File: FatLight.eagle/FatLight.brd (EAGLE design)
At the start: 75 x 100 mm, 27 parts, among them J1 12V, Q1 IRF540, Q2 IRF540, Q3 IRF540, Q4 16MHz, U1 ATMEGA328P-PU

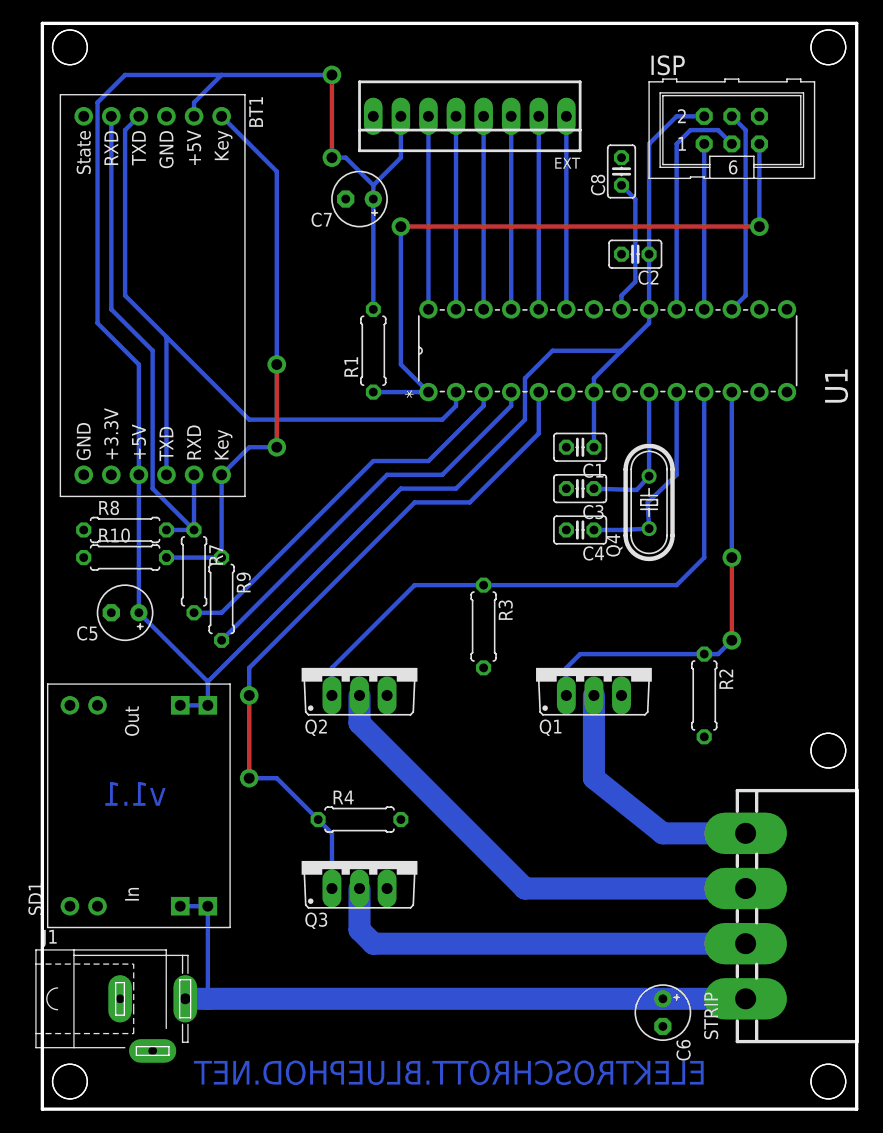
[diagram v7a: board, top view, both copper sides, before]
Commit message: Neue Revision des Boards, Firmware mit Farbeffekten
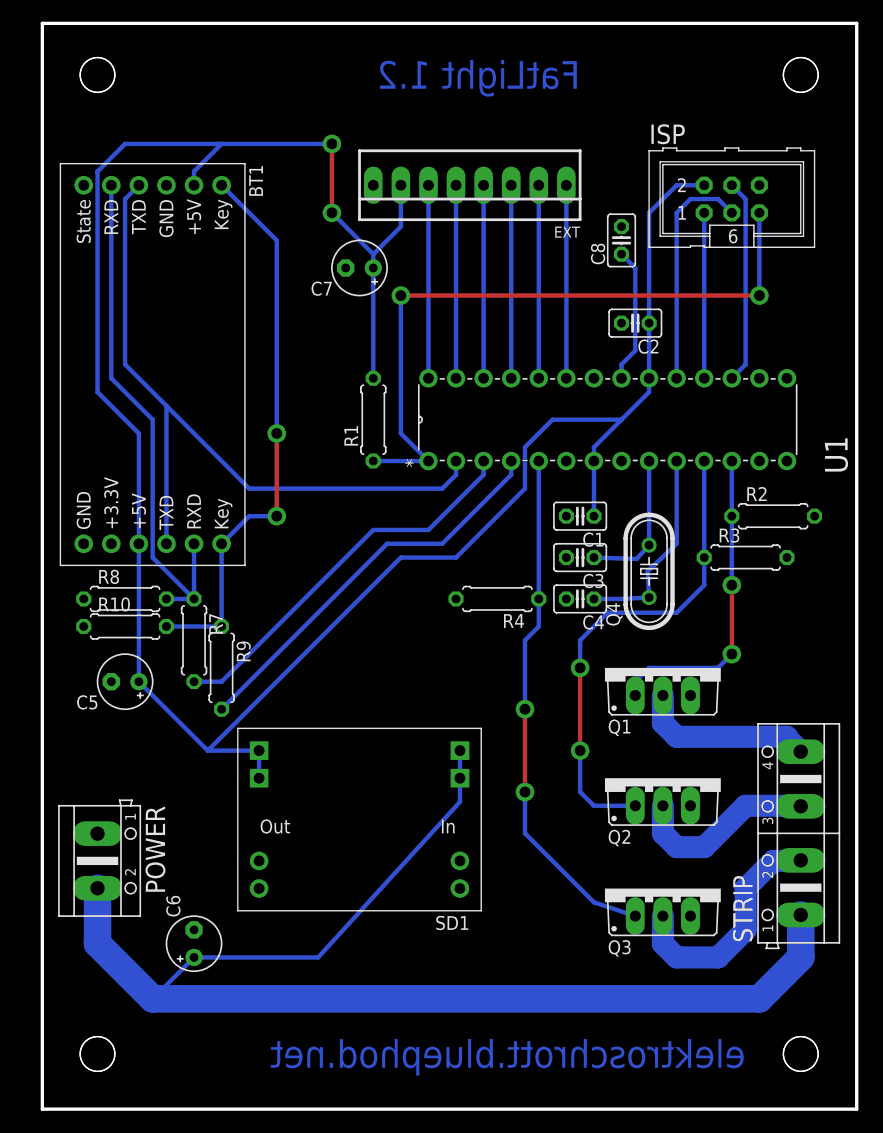
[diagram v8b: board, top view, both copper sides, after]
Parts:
- removed J1: 12V, con-jack:SPC4077
- added POWER: (no value), con-ptr500:AK500/2
- STRIP: device con-amp:FLOP-4V -> con-ptr500:AK500/4
- moved C6 43.6 mm to (14.0, 15.2), turned to 90 degrees
- moved Q2 29.7 mm to (57.1, 30.5)
- moved Q3 28.1 mm to (57.1, 20.3)
- moved R3 25.0 mm to (64.8, 50.8), turned to 0 degrees
- moved R4 24.0 mm to (41.9, 47.0), turned to 180 degrees
- moved SD1 20.4 mm to (29.2, 26.7), turned to 180 degrees
- moved R2 17.7 mm to (67.3, 54.6), turned to 0 degrees
- moved STRIP 9.16 mm to (69.8, 25.4)
- moved BT1 6.35 mm to (10.2, 68.6)
- moved ISP 6.35 mm to (63.5, 83.8)
- moved C1 6.35 mm to (49.5, 54.6)
- moved C3 6.35 mm to (49.5, 50.8)
- moved C4 6.35 mm to (49.5, 47.0)
- moved C5 6.35 mm to (7.62, 39.4)
- moved Q1 6.35 mm to (57.1, 40.6)
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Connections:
- net +12V: now also POWER.2, STRIP.1; no longer J1.3, STRIP.4
- net GND: now also POWER.1; no longer J1.1, J1.2
- net STRIP_BLU: now also STRIP.2; no longer STRIP.3
- net STRIP_GRN: now also STRIP.3; no longer STRIP.2
- net STRIP_RED: now also STRIP.4; no longer STRIP.1
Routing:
- net +12V: track 62.7 -> 118.4 mm
- net STRIP_GRN: track 44.4 -> 17.4 mm
- net STRIP_BLU: track 39.9 -> 21.7 mm
- net PWM_BLU: track 64.4 -> 47.8 mm
- net PWM_RED: track 41.7 -> 29.0 mm
- net PWM_GRN: track 56.3 -> 44.5 mm, vias 0 -> 2
- net STRIP_RED: track 23.4 -> 16.4 mm
- net +5V: track 210.2 -> 212.0 mm
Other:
- outline, holes or cut-outs redrawn
- board text added: "FatLight 1.2"
- board text added: "elektroschrott.bluephod.net"
- board text removed: "ELEKTROSCHROTT.BLUEPHOD.NET"
- board text removed: "v1.1"
